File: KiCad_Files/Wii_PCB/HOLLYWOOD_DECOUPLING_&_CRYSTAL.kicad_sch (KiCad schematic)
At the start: 60 parts, among them U5 27M

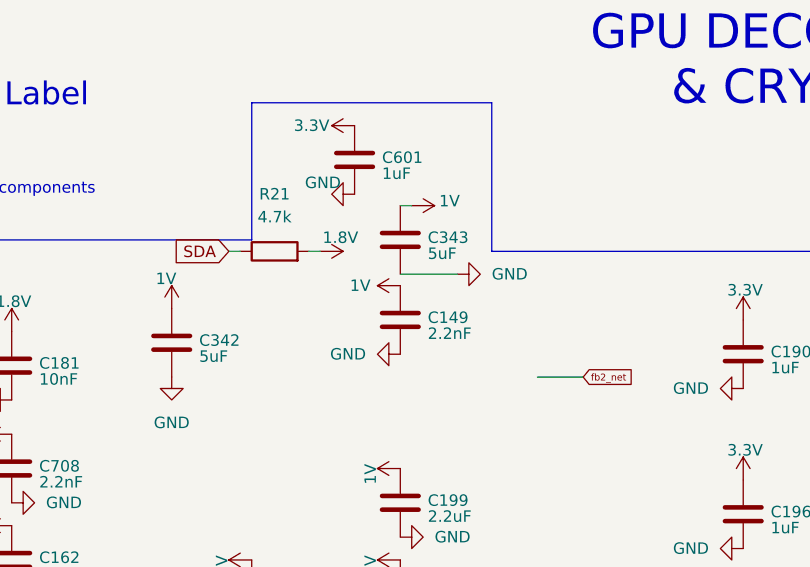
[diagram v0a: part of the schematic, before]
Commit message: Updated RAM & GPU bus to allow custom net rules for measuring intra-track spacing, added pad for reset, removed debug pads, reorganized ram schematic to cluster length matched signals, changed MX chip and U10 symbols, and re-labeled the wifi net interface.
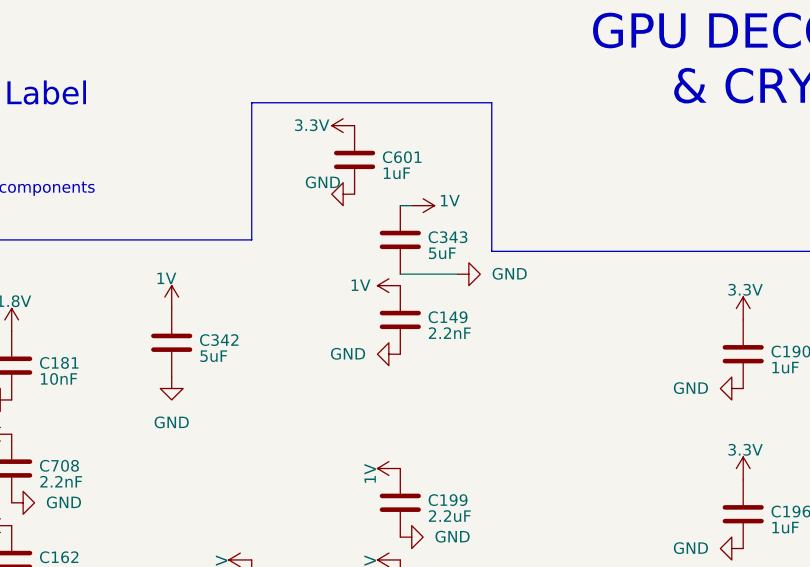
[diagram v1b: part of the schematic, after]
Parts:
- removed R21: 4.7k, Resistor_SMD:R_0402_1005Metric, symbol Device:R
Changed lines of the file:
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@@
 		)
 	)
-	(wire
-		(pts
-			(xy 86.36 55.88) (xy 87.63 55.88)
-		)
-		(stroke
-			(width 0)
-			(type default)
-		)
-	)
 	(polyline
 		(pts
@@
 	(wire
 		(pts
-			(xy 95.25 55.88) (xy 96.52 55.88)
-		)
-		(stroke
-			(width 0)
-			(type default)
-		)
-	)
-	(wire
-		(pts
 			(xy 156.21 214.63) (xy 156.21 217.17)
 		)
@@
 		)
 	)
-	(wire
-		(pts
-			(xy 120.65 69.85) (xy 125.73 69.85)
-		)
-		(stroke
-			(width 0)
-			(type default)
-		)
-	)
 	(polyline
 		(pts
@@
 		)
 	)
-	(global_label "SDA"
-		(shape input)
-		(at 86.36 55.88 180)
-		(fields_autoplaced yes)
-		(effects
-			(font
-				(size 1.27 1.27)
-			)
-			(justify right)
-		)
-		(property "Intersheetrefs" "${INTERSHEET_REFS}"
-			(at 79.8067 55.88 0)
-			(effects
-				(font
-					(size 1.27 1.27)
-				)
-				(justify right)
-			)
-		)
-	)
 	(global_label "XTALOUT"
 		(shape input)
@@
 		)
 	)
-	(global_label "fb2_net"
-		(shape input)
-		(at 125.73 69.85 0)
-		(fields_autoplaced yes)
-		(effects
-			(font
-				(size 0.762 0.762)
-			)
-			(justify left)
-		)
-		(property "Intersheetrefs" "${INTERSHEET_REFS}"
-			(at 131.7304 69.85 0)
-			(effects
-				(font
-					(size 1.27 1.27)
-				)
-				(justify left)
-			)
-		)
-	)
 	(symbol
 		(lib_id "Device:C")
@@
 	(symbol
 		(lib_id "power:VCC")
-		(at 96.52 55.88 270)
-		(unit 1)
-		(exclude_from_sim no)
-		(in_bom yes)
-		(on_board yes)
-		(dnp no)
-		(property "Reference" "#PWR0740"
-			(at 92.71 55.88 0)
-			(effects
-				(font
-					(size 1.27 1.27)
-				)
-				(hide yes)
-			)
-		)
-		(property "Value" "1.8V"
-			(at 96.774 54.356 90)
-			(effects
-				(font
-					(size 1.27 1.27)
-				)
-				(justify left)
-			)
-		)
-		(property "Footprint" ""
-			(at 96.52 55.88 0)
-			(effects
-				(font
-					(size 1.27 1.27)
-				)
-				(hide yes)
-			)
-		)
-		(property "Datasheet" ""
-			(at 96.52 55.88 0)
-			(effects
-				(font
-					(size 1.27 1.27)
-				)
-				(hide yes)
-			)
-		)
-		(property "Description" "Power symbol creates a global label with name \"VCC\""
-			(at 96.52 55.88 0)
-			(effects
-				(font
-					(size 1.27 1.27)
-				)
-				(hide yes)
-			)
-		)
-		(pin "1"
-		)
-		(instances
-			(project "Wii PCB"
-				(path "/07becb85-5b32-497c-802d-66c73e9db46a/a16de3f9-3a8b-4f3b-9109-039936b1b0ef"
-					(reference "#PWR0740")
-					(unit 1)
-				)
-			)
-		)
-	)
-	(symbol
-		(lib_id "power:VCC")
 		(at 106.68 50.8 270)
 		(unit 1)
@@
 					(unit 1)
 				)
-			)
-		)
-	)
-	(symbol
-		(lib_id "Device:R")
-		(at 91.44 55.88 90)
-		(unit 1)
-		(exclude_from_sim no)
-		(in_bom yes)
-		(on_board yes)
-		(dnp no)
-		(fields_autoplaced yes)
-		(property "Reference" "R21"
-			(at 91.44 49.53 90)
-			(effects
-				(font
-					(size 1.27 1.27)
-				)
-			)
-		)
-		(property "Value" "4.7k"
-			(at 91.44 52.07 90)
-			(effects
-				(font
-					(size 1.27 1.27)
-				)
-			)
-		)
-		(property "Footprint" "Resistor_SMD:R_0402_1005Metric"
-			(at 91.44 57.658 90)
-			(effects
-				(font
-					(size 1.27 1.27)
-				)
-				(hide yes)
-			)
-		)
-		(property "Datasheet" "~"
-			(at 91.44 55.88 0)
-			(effects
-				(font
-					(size 1.27 1.27)
-				)
-				(hide yes)
-			)
-		)
-		(property "Description" "Resistor"
-			(at 91.44 55.88 0)
-			(effects
-				(font
-					(size 1.27 1.27)
-				)
-				(hide yes)
-			)
-		)
-		(pin "1"
-		)
-		(pin "2"
-		)
-		(instances
-			(project "Wii PCB"
-				(path "/07becb85-5b32-497c-802d-66c73e9db46a/a16de3f9-3a8b-4f3b-9109-039936b1b0ef"
-					(reference "R21")
-					(unit 1)
-				)
